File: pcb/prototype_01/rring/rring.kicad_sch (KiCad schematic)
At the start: 61 parts, among them SW1 Button, U1 DA14531-00000OG2, U2 ADP160ACBZ-1.8-R7, U3 ICM-20948, U4 LTC4124EV-TRMPBF, U5 TCA6418EYFPR, Y1 32MHz

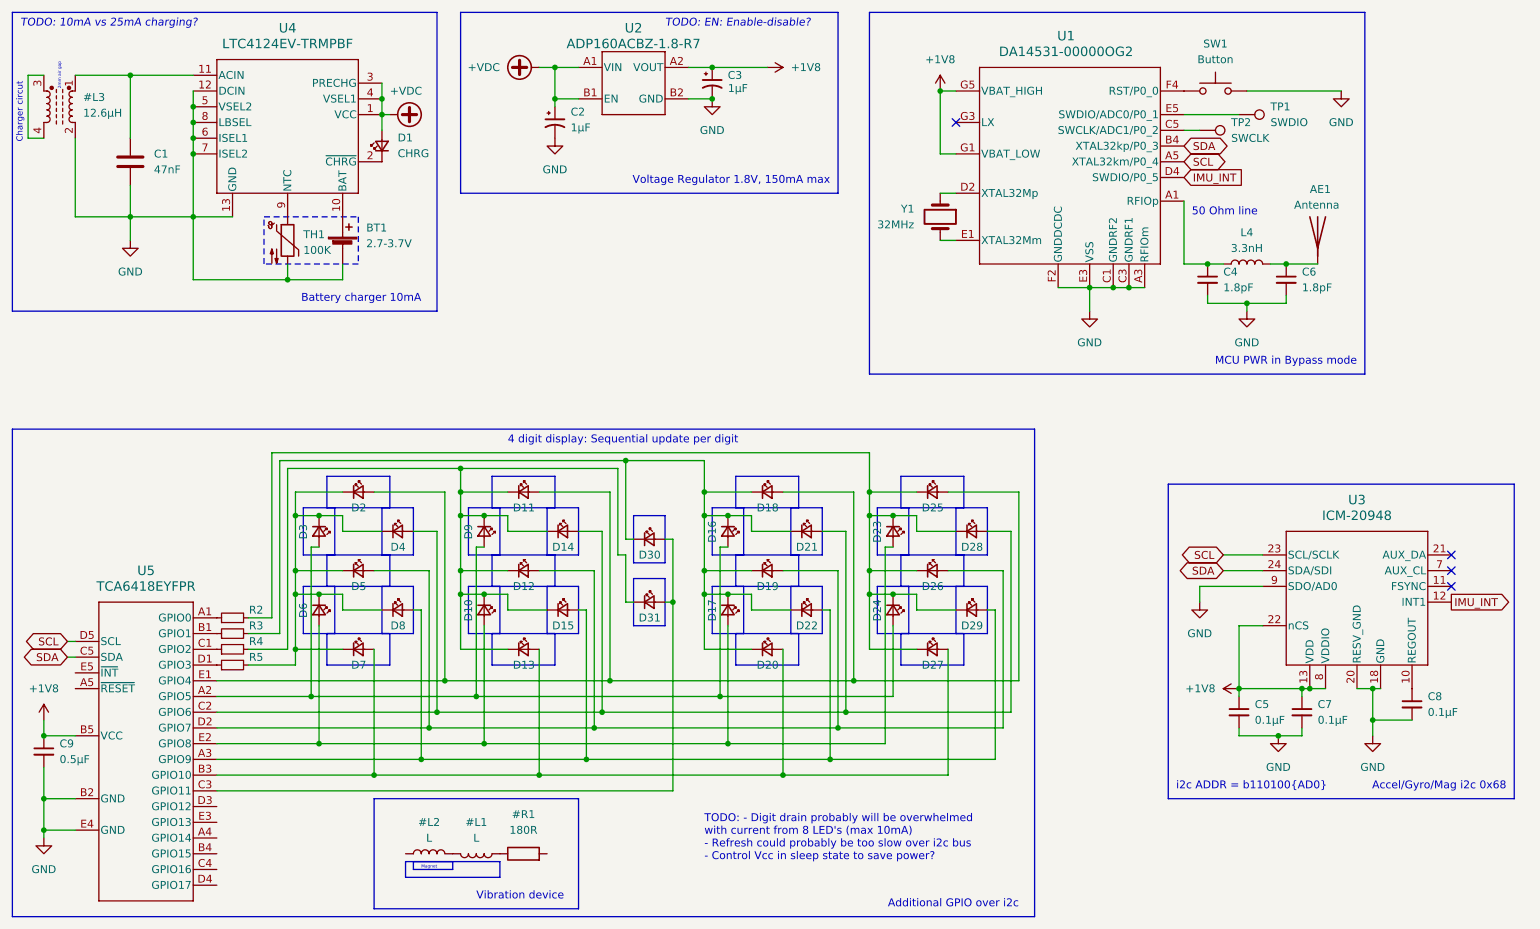
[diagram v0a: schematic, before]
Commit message: Completed the main PCB of the first prototype
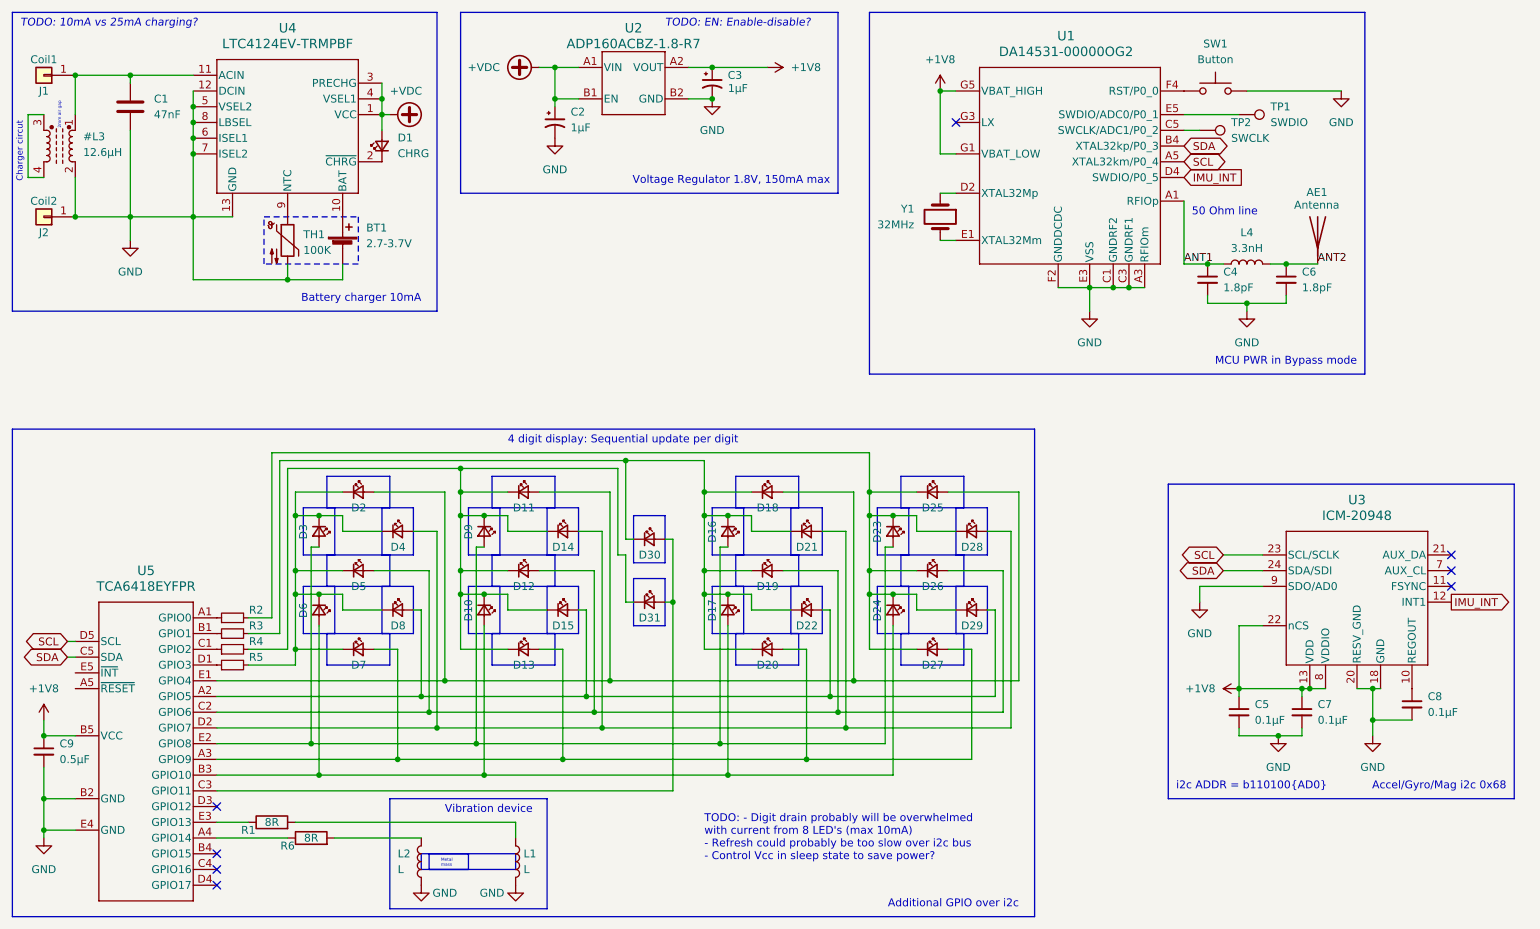
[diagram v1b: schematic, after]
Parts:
- added J1: Coil1, footprints:Conn_Pad_0.5x0.5mm, symbol Connector_Generic:Conn_01x01
- added J2: Coil2, footprints:Conn_Pad_0.5x0.5mm, symbol Connector_Generic:Conn_01x01
- added R6: 8R, Resistor_SMD:R_0201_0603Metric, symbol Device:R
- L1: renamed from #L1; footprint (none) -> Inductor_SMD:L_0805_2012Metric
- L2: renamed from #L2; footprint (none) -> Inductor_SMD:L_0805_2012Metric
- R1: renamed from #R1; value 180R -> 8R
- TP1, TP2: footprint TestPoint:TestPoint_Pad_D1.0mm -> footprints:TestPoint_Pad_D0.5mm
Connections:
- net GND: now also L1.2, L2.1, J2.1 (Pin_1)
- net at D16.2 (A), D3.2 (A), D9.2 (A): now also D23.2 (A), U5.E2 (GPIO8); no longer D24.2 (A), U5.A2 (GPIO5)
- net ANT1: now reaches C4.1, L4.1, U1.A1 (RFIOp)
- net at D13.2 (A), D20.2 (A), D27.2 (A)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: now also U5.A3 (GPIO9); no longer U5.B3 (GPIO10)
- net at D10.2 (A), D17.2 (A), D6.2 (A): now also D24.2 (A), U5.B3 (GPIO10); no longer D23.2 (A), U5.E2 (GPIO8)
- net ANT2: now reaches AE1.1 (A), C6.1, L4.2
- net at D12.2 (A), D19.2 (A), D26.2 (A)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: now also U5.C2 (GPIO6); no longer U5.D2 (GPIO7)
- net at D14.2 (A), D21.2 (A), D28.2 (A)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: now also U5.D2 (GPIO7); no longer U5.C2 (GPIO6)
- net at D15.2 (A), D22.2 (A), D29.2 (A)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: now also U5.A2 (GPIO5); no longer U5.A3 (GPIO9)
- net at #L3.1, C1.1, U4.11 (ACIN): now also J1.1 (Pin_1)
- net at L2.2: now also R6.2; no longer L1.2
- net at R1.1: now also U5.E3 (GPIO13); no longer L1.1
- net at R1.2: now also L1.1
- net at U5.A4 (GPIO14): now also R6.1
- no-connect marks 4 -> 8
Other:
- note added: "Metal mass"
- note removed: "Magnet"
- moved on the sheet: C1
